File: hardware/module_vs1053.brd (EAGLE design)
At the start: 109.9 x 68.6 mm, 125 parts, among them IC1 IC_USBLC6-2, IC2 LM1117IMPX-3.3, IC3 PIC32MX795F512, IC4 DP83848, IC5 LM1117MPX-2.5, J1 AUDIO_JACK_TRRSSMD_RA, U1 USD-SOCKETUSD, U3 VS1053-L, X2 CRYSTALS-NOGND-CFPX-217, X3 KUSBVX, Y3 CRYSTAL-GROUNDEDSMD-5X3.2

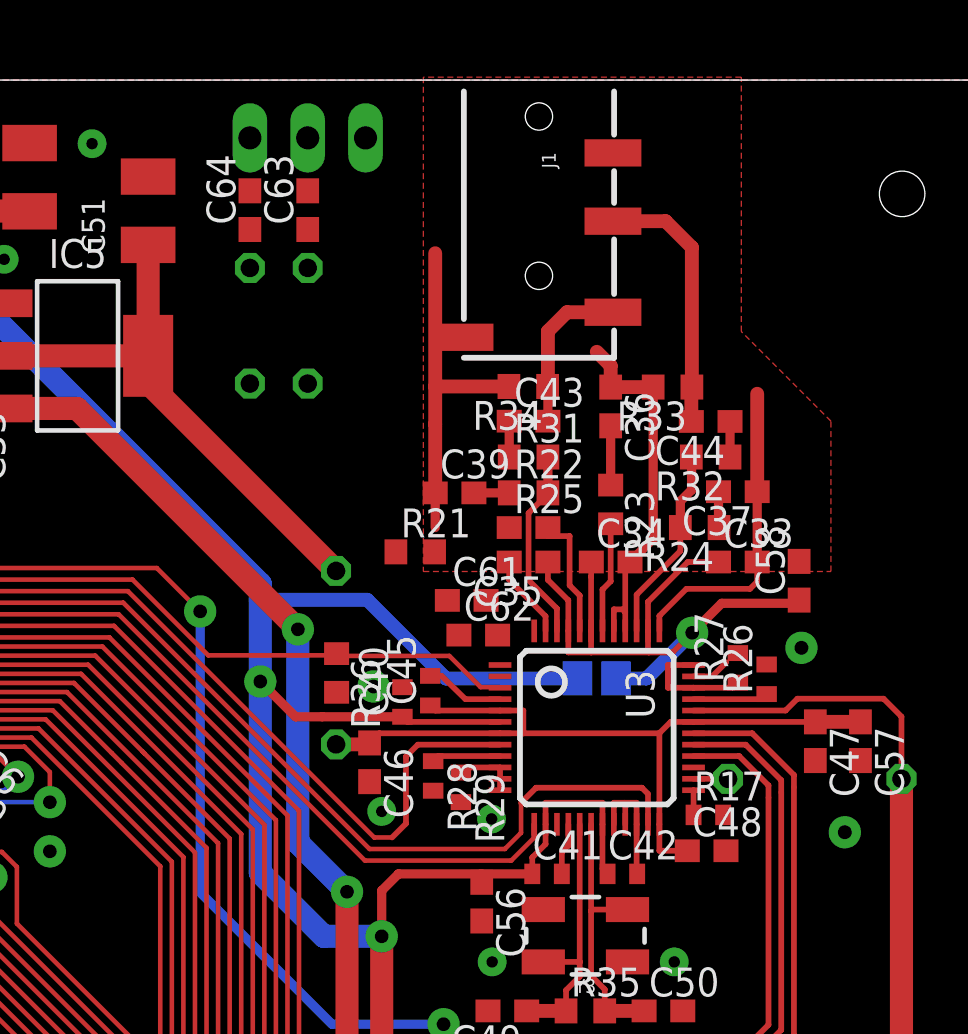
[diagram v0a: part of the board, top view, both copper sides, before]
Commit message: Line input added
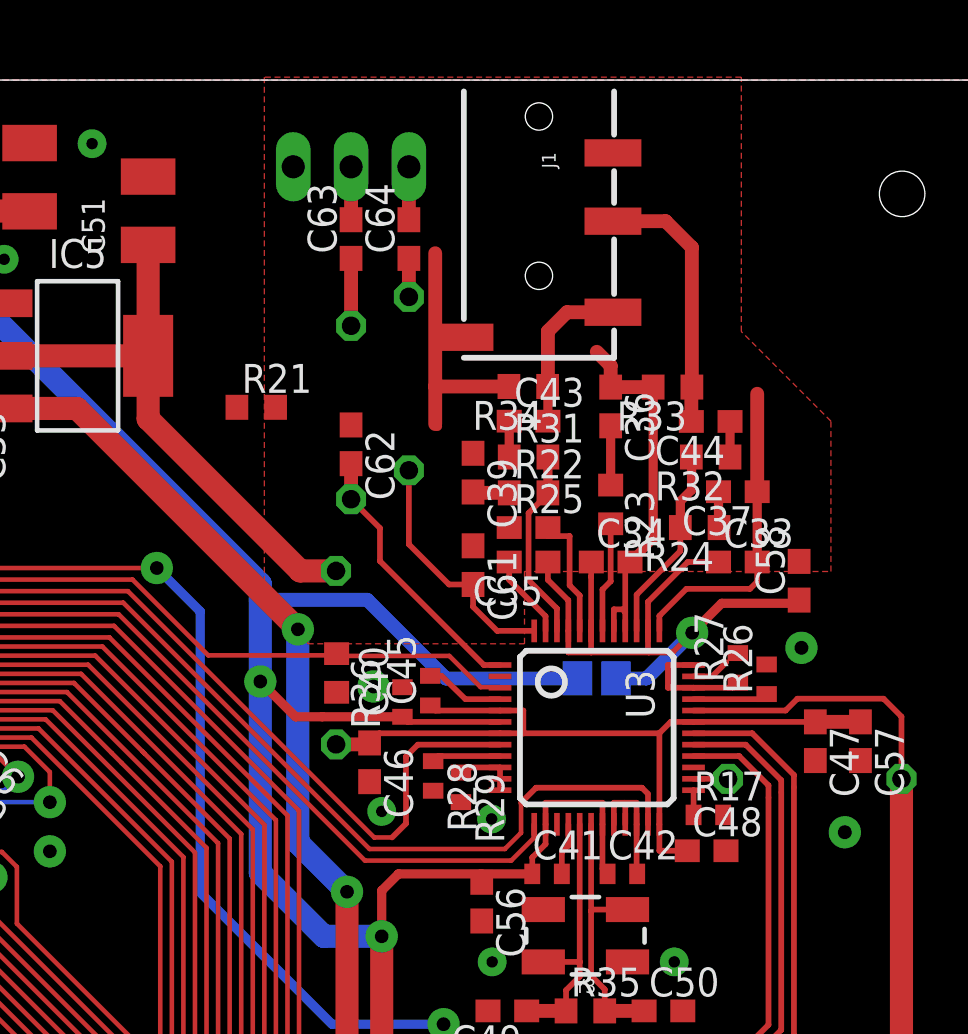
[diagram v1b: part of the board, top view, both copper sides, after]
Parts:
- R12, R37: device rcl:0204/5 -> rcl:0204/7
- moved C62 10.1 mm to (80.6, 52.6), turned to 270 degrees
- moved R21 9.44 mm to (76.5, 54.2)
- moved R37 7.43 mm to (83.2, 55.2)
- moved C64 7.10 mm to (83.2, 61.6)
- moved R12 4.26 mm to (80.6, 54.0)
- moved JP1 2.29 mm to (80.6, 64.8), turned to 0 degrees
- moved C63 2.29 mm to (80.6, 61.6)
- moved C61 1.57 mm to (86.0, 47.3), turned to 270 degrees
- moved C39 1.20 mm to (86.0, 51.3), turned to 270 degrees
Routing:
- net N$13: track 0.00 -> 12.0 mm
- net N$5: track 0.00 -> 10.9 mm
- net VS_AGND: track 49.3 -> 44.8 mm
- net N$15: track 0.00 -> 2.96 mm
- net IN_RIGHT: track 0.00 -> 2.32 mm
- net IN_LEFT: track 0.00 -> 2.32 mm
- net N$14: track 0.00 -> 1.69 mm
- net _1V8: track 26.6 -> 27.5 mm
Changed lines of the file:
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@@
 <element name="C30" library="rcl" package="SMC_A" value="" x="97.1804" y="15.1638" rot="R180"/>
 <element name="R18" library="rcl" package="R0805" value="" x="43.18" y="46.99" rot="R270"/>
-<element name="R21" library="rcl" package="R0603" value="" x="83.4644" y="47.8536"/>
+<element name="R21" library="rcl" package="R0603" value="" x="76.4794" y="54.2036"/>
 <element name="C33" library="rcl" package="C0603" value="100n" x="97.6376" y="47.407"/>
 <element name="C34" library="rcl" package="C0603" value="100n" x="92.0496" y="47.407"/>
@@
 <element name="C36" library="rcl" package="C0603" value="47n" x="92.0496" y="54.2408" rot="R270"/>
 <element name="C37" library="rcl" package="C0603" value="10n" x="97.6376" y="50.4952" rot="R180"/>
-<element name="C39" library="rcl" package="C0603" value="10n" x="85.1916" y="50.4444"/>
+<element name="C39" library="rcl" package="C0603" value="10n" x="86.0044" y="51.3334" rot="R270"/>
 <element name="R26" library="rcl" package="R0402" value="100k" x="98.9022" y="42.255440625" rot="R90"/>
 <element name="R27" library="rcl" package="R0402" value="100k" x="97.6376" y="42.75581875" rot="R90"/>
@@
 <attribute name="PROD_ID" value="CONN-10676" x="88.9" y="68.58" size="1.778" layer="27" rot="R270" display="off"/>
 </element>
-<element name="C61" library="rcl" package="C0603" value="10n" x="85.725" y="45.72"/>
-<element name="C62" library="rcl" package="C0603" value="10n" x="86.233" y="44.196"/>
-<element name="R12" library="rcl" package="0204/5" value="470" x="78.74" y="57.785" rot="MR270"/>
-<element name="R37" library="rcl" package="0204/5" value="470" x="76.2" y="57.785" rot="MR270"/>
-<element name="C63" library="rcl" package="C0603" value="1u" x="78.74" y="62.865" rot="R90"/>
-<element name="C64" library="rcl" package="C0603" value="1u" x="76.2" y="62.865" rot="R90"/>
-<element name="JP1" library="pinhead" package="1X03" value="" x="78.74" y="66.04" rot="MR180"/>
+<element name="C61" library="rcl" package="C0603" value="10n" x="86.0044" y="47.2694" rot="R270"/>
+<element name="C62" library="rcl" package="C0603" value="10n" x="80.645" y="52.578" rot="R270"/>
+<element name="R12" library="rcl" package="0204/7" value="470" x="80.645" y="53.975" rot="MR270"/>
+<element name="R37" library="rcl" package="0204/7" value="470" x="83.185" y="55.245" rot="MR270"/>
+<element name="C63" library="rcl" package="C0603" value="1u" x="80.645" y="61.595" rot="R90"/>
+<element name="C64" library="rcl" package="C0603" value="1u" x="83.185" y="61.595" rot="R90"/>
+<element name="JP1" library="pinhead" package="1X03" value="" x="80.645" y="64.77" rot="MR0"/>
 </elements>
 <signals>
@@
 <contactref element="IC3" pad="9"/>
 <wire x1="51.892" y1="48.7424" x2="54.3306" y2="51.181" width="0.2032" layer="1"/>
-<via x="74.0156" y="45.2374" extent="1-16" drill="0.6" diameter="1.4224" shape="octagon"/>
+<via x="72.1106" y="47.1424" extent="1-16" drill="0.6" diameter="1.4224" shape="octagon"/>
 <wire x1="100.1014" y1="37.5158" x2="100.1014" y2="26.6192" width="0.254" layer="1"/>
 <wire x1="100.1014" y1="26.6192" x2="96.9772" y2="23.495" width="0.254" layer="1"/>
@@
 <wire x1="54.3306" y1="51.181" x2="59.5884" y2="51.181" width="0.2032" layer="1"/>
 <wire x1="59.5884" y1="51.181" x2="63.627" y2="47.1424" width="0.2032" layer="1"/>
-<wire x1="74.0156" y1="45.2374" x2="74.0156" y2="32.893" width="0.4064" layer="16"/>
 <wire x1="74.0156" y1="32.893" x2="79.8068" y2="27.1018" width="0.4064" layer="16"/>
 <wire x1="84.709" y1="27.1018" x2="79.8068" y2="27.1018" width="0.4064" layer="16"/>
@@
 <wire x1="87.757" y1="22.7584" x2="88.4936" y2="23.495" width="0.254" layer="1"/>
 <wire x1="63.627" y1="47.1424" x2="72.1106" y2="47.1424" width="0.2032" layer="1"/>
-<wire x1="72.1106" y1="47.1424" x2="74.0156" y2="45.2374" width="0.2032" layer="1"/>
+<wire x1="74.0156" y1="32.893" x2="74.0156" y2="45.2374" width="0.4064" layer="16"/>
+<wire x1="74.0156" y1="45.2374" x2="72.1106" y2="47.1424" width="0.4064" layer="16"/>
 </signal>
 <signal name="VS_MOSI">
@@
 <wire x1="98.4876" y1="46.5446" x2="98.171" y2="46.228" width="0.251459375" layer="1"/>
 <wire x1="98.171" y1="46.228" x2="95.377" y2="46.228" width="0.251459375" layer="1"/>
-<wire x1="84.3416" y1="50.4444" x2="84.3416" y2="53.467" width="0.6096" layer="1"/>
 <contactref element="R34" pad="2"/>
 <contactref element="R33" pad="2"/>
@@
 <wire x1="93.9174" y1="48.4248" x2="92.8996" y2="47.407" width="0.4064" layer="1"/>
 <wire x1="84.3416" y1="55.118" x2="84.3416" y2="60.9736" width="0.6096" layer="1"/>
-<wire x1="84.3416" y1="48.9204" x2="84.3416" y2="50.4444" width="0.4064" layer="1"/>
 <wire x1="87.5801" y1="55.118" x2="84.3416" y2="55.118" width="0.6096" layer="1"/>
 <wire x1="93.9174" y1="55.0926" x2="93.9174" y2="48.4248" width="0.4064" layer="1"/>
@@
 <wire x1="98.4876" y1="50.4952" x2="98.4876" y2="54.7996" width="0.6096" layer="1"/>
 <polygon width="0.4064" layer="1" isolate="0.3048" thermals="no">
-<vertex x="83.82" y="68.707"/>
-<vertex x="83.82" y="46.99"/>
+<vertex x="76.835" y="68.707"/>
+<vertex x="76.835" y="46.355"/>
+<vertex x="78.74" y="44.45"/>
+<vertex x="78.74" y="43.815"/>
+<vertex x="88.265" y="43.815"/>
+<vertex x="88.265" y="46.99"/>
 <vertex x="101.727" y="46.99"/>
 <vertex x="101.727" y="53.594"/>
@@
 <contactref element="R25" pad="1"/>
 <contactref element="C62" pad="1"/>
-<wire x1="84.3416" y1="60.9736" x2="81.28" y2="66.04" width="0" layer="19" extent="1-1"/>
-<wire x1="84.875" y1="45.72" x2="84.3144" y2="47.8536" width="0" layer="19" extent="1-1"/>
-<wire x1="85.383" y1="44.196" x2="84.875" y2="45.72" width="0" layer="19" extent="1-1"/>
 </signal>
 <signal name="VS_CVDD">
@@
 <wire x1="65.5288" y1="56.4612" x2="65.5318" y2="56.4642" width="0.8128" layer="1"/>
 <wire x1="71.7298" y1="56.4642" x2="71.7298" y2="61.3396" width="1.016" layer="1"/>
-<wire x1="79.9848" y1="47.0154" x2="71.7298" y2="55.2704" width="1.016" layer="1"/>
-<wire x1="71.7298" y1="55.2704" x2="71.7298" y2="56.4642" width="1.016" layer="1"/>
+<wire x1="71.7298" y1="56.4642" x2="71.7298" y2="53.6954" width="1.016" layer="1"/>
+<wire x1="71.7298" y1="53.6954" x2="78.4098" y2="47.0154" width="1.016" layer="1"/>
+<wire x1="79.9848" y1="47.0154" x2="78.4098" y2="47.0154" width="1.016" layer="1"/>
 </signal>
 <signal name="VS_N$14">
@@
 <contactref element="R22" pad="1"/>
 <contactref element="C39" pad="2"/>
-<wire x1="86.0416" y1="50.4444" x2="87.5928" y2="50.4444" width="0.4064" layer="1"/>
+<wire x1="87.5928" y1="50.4444" x2="86.0434" y2="50.4444" width="0.6096" layer="1"/>
+<wire x1="86.0434" y1="50.4444" x2="86.0044" y2="50.4834" width="0.6096" layer="1"/>
 </signal>
 <signal name="VS_N$9">
@@
 <contactref element="R37" pad="2"/>
 <contactref element="U3" pad="48"/>
-<wire x1="88.69" y1="44.382" x2="86.575" y2="45.72" width="0" layer="19" extent="1-1"/>
-<wire x1="76.2" y1="55.245" x2="86.575" y2="45.72" width="0" layer="19" extent="1-1"/>
+<wire x1="83.185" y1="51.435" x2="83.185" y2="48.1838" width="0.251459375" layer="1"/>
+<wire x1="83.185" y1="48.1838" x2="84.9494" y2="46.4194" width="0.251459375" layer="1"/>
+<wire x1="84.9494" y1="46.4194" x2="86.0044" y2="46.4194" width="0.251459375" layer="1"/>
+<wire x1="88.69" y1="44.382" x2="87.063" y2="44.382" width="0.251459375" layer="1"/>
+<wire x1="86.0044" y1="46.4194" x2="86.0044" y2="45.4406" width="0.251459375" layer="1"/>
+<wire x1="86.0044" y1="45.4406" x2="87.063" y2="44.382" width="0.251459375" layer="1"/>
 </signal>
 <signal name="N$13">
@@
 <contactref element="R12" pad="2"/>
 <contactref element="U3" pad="1"/>
-<wire x1="87.083" y1="44.196" x2="78.74" y2="55.245" width="0" layer="19" extent="1-1"/>
-<wire x1="87.19" y1="42.882" x2="87.083" y2="44.196" width="0" layer="19" extent="1-1"/>
+<wire x1="81.915" y1="47.4472" x2="86.4802" y2="42.882" width="0.251459375" layer="1"/>
+<wire x1="87.19" y1="42.882" x2="86.4802" y2="42.882" width="0.251459375" layer="1"/>
+<wire x1="81.915" y1="47.4472" x2="81.915" y2="48.895" width="0.251459375" layer="1"/>
+<wire x1="81.915" y1="48.895" x2="80.645" y2="50.165" width="0.251459375" layer="1"/>
+<wire x1="80.645" y1="50.165" x2="80.645" y2="51.728" width="0.6096" layer="1"/>
 </signal>
 <signal name="N$14">
 <contactref element="R37" pad="1"/>
 <contactref element="C64" pad="1"/>
-<wire x1="76.2" y1="60.325" x2="76.2" y2="62.015" width="0" layer="19" extent="1-1"/>
+<wire x1="83.185" y1="60.745" x2="83.185" y2="59.055" width="0.6096" layer="1"/>
 </signal>
 <signal name="N$15">
 <contactref element="R12" pad="1"/>
 <contactref element="C63" pad="1"/>
-<wire x1="78.74" y1="60.325" x2="78.74" y2="62.015" width="0" layer="19" extent="1-1"/>
+<wire x1="80.645" y1="57.785" x2="80.645" y2="60.745" width="0.6096" layer="1"/>
 </signal>
 <signal name="IN_LEFT">
 <contactref element="JP1" pad="2"/>
 <contactref element="C63" pad="2"/>
-<wire x1="78.74" y1="63.715" x2="78.74" y2="66.04" width="0" layer="19" extent="1-1"/>
+<wire x1="80.645" y1="62.445" x2="80.645" y2="64.77" width="0.6096" layer="1"/>
 </signal>
 <signal name="IN_RIGHT">
 <contactref element="C64" pad="2"/>
 <contactref element="JP1" pad="1"/>
-<wire x1="76.2" y1="63.715" x2="76.2" y2="66.04" width="0" layer="19" extent="1-1"/>
+<wire x1="83.185" y1="62.445" x2="83.185" y2="64.77" width="0.6096" layer="1"/>
 </signal>
 </signals>

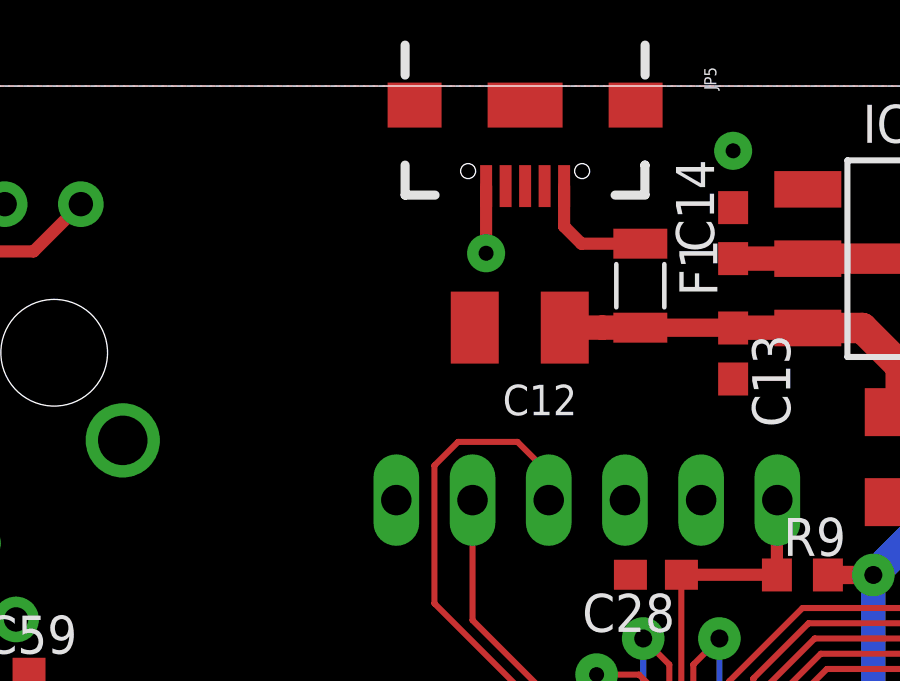
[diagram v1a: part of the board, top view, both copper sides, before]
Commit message: Alternate power connector added
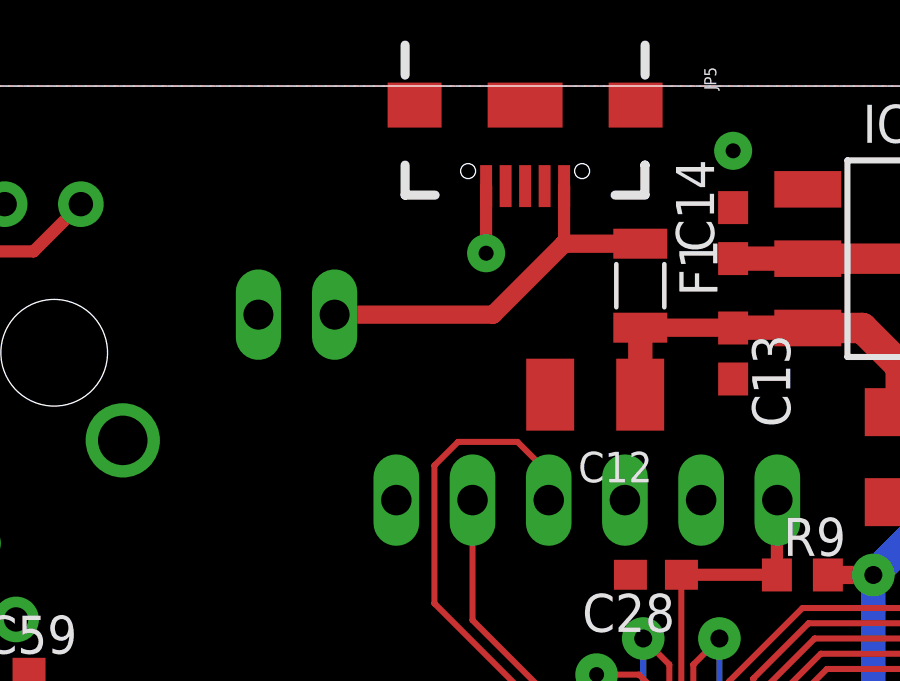
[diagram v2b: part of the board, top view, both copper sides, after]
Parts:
- added X1: 22-23-2021, con-molex:22-23-2021
- moved C12 3.36 mm to (47.4, 58.3)
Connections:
- net GND: now also X1.2
- net N$17: now also X1.1
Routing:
- net N$17: track 4.12 -> 13.1 mm
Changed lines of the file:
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@@
 <element name="JP3" library="pinhead" package="1X04" value="" x="36.6014" y="26.0604" rot="MR270"/>
 <element name="IC3" library="DodoMicroR3" package="TQFP100_12X12" value="PIC32MX795F512" x="50.292" y="39.2938" rot="R180"/>
-<element name="C12" library="rcl" package="SMC_B" value="" x="44.9072" y="60.5282" rot="R180"/>
+<element name="C12" library="rcl" package="SMC_B" value="" x="47.4218" y="58.293" rot="R180"/>
 <element name="C13" library="rcl" package="C0603" value="" x="52.0192" y="59.6646" rot="R270"/>
 <element name="C14" library="rcl" package="C0603" value="" x="52.0192" y="63.6778" rot="R90"/>
@@
 <element name="C64" library="rcl" package="C0603" value="1u" x="83.185" y="61.595" rot="R90"/>
 <element name="JP1" library="pinhead" package="1X03" value="" x="80.645" y="64.77" rot="MR0"/>
+<element name="X1" library="con-molex" package="22-23-2021" value="22-23-2021" x="37.465" y="60.96" rot="MR0">
+<attribute name="OC_NEWARK" value="25C3832" x="45.085" y="72.39" size="1.778" layer="28" rot="MR0" display="off"/>
+<attribute name="MPN" value="22-23-2021" x="45.085" y="72.39" size="1.778" layer="28" rot="MR0" display="off"/>
+<attribute name="MF" value="MOLEX" x="45.085" y="72.39" size="1.778" layer="28" rot="MR0" display="off"/>
+<attribute name="OC_FARNELL" value="1462926" x="45.085" y="72.39" size="1.778" layer="28" rot="MR0" display="off"/>
+</element>
 </elements>
 <signals>
@@
 <wire x1="96.5094" y1="42.382" x2="97.1296" y2="43.0022" width="0.251459375" layer="1"/>
 <contactref element="R17" pad="2"/>
+<contactref element="X1" pad="2"/>
 </signal>
 <signal name="A3V">
@@
 <contactref element="F1" pad="2"/>
 <contactref element="C30" pad="+"/>
-<wire x1="46.4072" y1="60.5282" x2="47.655" y2="60.5282" width="0.8128" layer="1"/>
-<wire x1="47.655" y1="60.5282" x2="48.925" y2="60.5252" width="0.8128" layer="1"/>
 <wire x1="48.925" y1="60.5252" x2="52.07" y2="60.5252" width="0.6096" layer="1"/>
 <wire x1="52.07" y1="60.5252" x2="54.498" y2="60.5252" width="0.8128" layer="1"/>
@@
 <wire x1="65.5318" y1="54.1532" x2="68.605" y2="54.1532" width="1.016" layer="1"/>
 <wire x1="68.605" y1="54.1532" x2="78.3082" y2="44.45" width="1.016" layer="1"/>
+<wire x1="48.925" y1="60.5252" x2="48.925" y2="58.2962" width="0.8128" layer="1"/>
+<wire x1="48.925" y1="58.2962" x2="48.9218" y2="58.293" width="0.8128" layer="1"/>
 </signal>
 <signal name="D2_P">
@@
 <contactref element="JP5" pad="VBUS1"/>
 <contactref element="F1" pad="1"/>
-<wire x1="46.385" y1="65.245" x2="46.385" y2="63.9018" width="0.4064" layer="1"/>
-<wire x1="46.385" y1="63.9018" x2="46.9616" y2="63.3252" width="0.4064" layer="1"/>
-<wire x1="48.925" y1="63.3252" x2="46.9616" y2="63.3252" width="0.4064" layer="1"/>
+<wire x1="46.385" y1="65.245" x2="46.385" y2="63.3252" width="0.4064" layer="1"/>
+<wire x1="48.925" y1="63.3252" x2="46.385" y2="63.3252" width="0.6096" layer="1"/>
+<wire x1="46.385" y1="63.3252" x2="46.3834" y2="63.3252" width="0.6096" layer="1"/>
+<wire x1="46.3834" y1="63.3252" x2="44.0182" y2="60.96" width="0.6096" layer="1"/>
+<wire x1="44.0182" y1="60.96" x2="38.735" y2="60.96" width="0.6096" layer="1"/>
+<contactref element="X1" pad="1"/>
 </signal>
 <signal name="N$36">
